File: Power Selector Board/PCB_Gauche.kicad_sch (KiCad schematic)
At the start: 23 parts, among them J101 MSD-DB01M-12P, J102 MSD-DB01F-12P_1, J103 64900221122, J104 64900221122, J105 64900221122, J106 1998865, K101 G6SK-2G DC24, K102 J115F11C24VDCSH.9, K103 J115F11C24VDCSH.9, U102 LMW78_24-0.3RL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

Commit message: Premier commit pour routing PCB. Modif footprint connecteur batterie.
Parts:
- added H1 (x4): Mounting-Hole-M3, Connectors:Mounting_Hole_3mm, symbol Mechanicals:Mounting-Hole-M3
- F101, F102: Current Rating (A) 30A -> 6.3A
- J101, J102: footprint Connectors:649012227222 -> Connectors:MSD-DB01F-12P-V2.0
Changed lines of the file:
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@@
       (effects (font (size 1.524 1.524)))
     )
-    (property "Footprint" "Connectors:649012227222" (at 335.28 146.05 0)
+    (property "Footprint" "Connectors:MSD-DB01F-12P-V2.0" (at 335.28 146.05 0)
       (effects (font (size 1.524 1.524)) hide)
     )
@@
     )
   )
+  (symbol (lib_id "Mechanicals:Mounting-Hole-M3") (at 58.42 203.2 0) (unit 1)
+    (in_bom yes) (on_board yes) (dnp no) (fields_autoplaced)
+    (property "Reference" "H1" (at 63.5 201.93 0)
+      (effects (font (size 1.524 1.524)) (justify left))
+    )
+    (property "Value" "Mounting-Hole-M3" (at 63.5 204.47 0)
+      (effects (font (size 1.524 1.524)) (justify left))
+    )
+    (property "Footprint" "Connectors:Mounting_Hole_3mm" (at 58.42 217.17 0)
+      (effects (font (size 1.524 1.524)) hide)
+    )
+    (property "Datasheet" "" (at 58.42 208.28 0)
+      (effects (font (size 1.524 1.524)) hide)
+    )
+    (pin "1")
+    (instances
+      (project "Power Selector"
+        (path "/809bdac1-fe7e-479d-b3c2-abd6ebce72b5/01a8522b-18e6-465b-b2cb-1d0f4aea8e80"
+          (reference "H1") (unit 1)
+        )
+        (path "/809bdac1-fe7e-479d-b3c2-abd6ebce72b5/c8dd6968-27fd-46e9-bc25-cf95ac0a1b0e"
+          (reference "H6") (unit 1)
+        )
+      )
+    )
+  )
   (symbol (lib_id "Power_Port:GND_G") (at 187.96 226.06 0) (unit 1)
     (in_bom yes) (on_board yes) (dnp no)
@@
         (path "/809bdac1-fe7e-479d-b3c2-abd6ebce72b5/c8dd6968-27fd-46e9-bc25-cf95ac0a1b0e"
           (reference "#PWR0205") (unit 1)
+        )
+      )
+    )
+  )
+  (symbol (lib_id "Mechanicals:Mounting-Hole-M3") (at 58.42 215.9 0) (unit 1)
+    (in_bom yes) (on_board yes) (dnp no) (fields_autoplaced)
+    (property "Reference" "H1" (at 63.5 214.63 0)
+      (effects (font (size 1.524 1.524)) (justify left))
+    )
+    (property "Value" "Mounting-Hole-M3" (at 63.5 217.17 0)
+      (effects (font (size 1.524 1.524)) (justify left))
+    )
+    (property "Footprint" "Connectors:Mounting_Hole_3mm" (at 58.42 229.87 0)
+      (effects (font (size 1.524 1.524)) hide)
+    )
+    (property "Datasheet" "" (at 58.42 220.98 0)
+      (effects (font (size 1.524 1.524)) hide)
+    )
+    (pin "1")
+    (instances
+      (project "Power Selector"
+        (path "/809bdac1-fe7e-479d-b3c2-abd6ebce72b5/01a8522b-18e6-465b-b2cb-1d0f4aea8e80"
+          (reference "H1") (unit 1)
+        )
+        (path "/809bdac1-fe7e-479d-b3c2-abd6ebce72b5/c8dd6968-27fd-46e9-bc25-cf95ac0a1b0e"
+          (reference "H7") (unit 1)
         )
       )
@@
       (effects (font (size 1.524 1.524)))
     )
-    (property "Footprint" "Connectors:649012227222" (at 53.34 153.67 0)
+    (property "Footprint" "Connectors:MSD-DB01F-12P-V2.0" (at 53.34 153.67 0)
       (effects (font (size 1.524 1.524)) hide)
     )
@@
       (effects (font (size 1.524 1.524)) hide)
     )
-    (property "Current Rating (A)" "30A" (at 67.31 72.39 0)
+    (property "Current Rating (A)" "6.3A" (at 67.31 72.39 0)
       (effects (font (size 1.27 1.27)))
     )
@@
     )
   )
+  (symbol (lib_id "Mechanicals:Mounting-Hole-M3") (at 58.42 228.6 0) (unit 1)
+    (in_bom yes) (on_board yes) (dnp no) (fields_autoplaced)
+    (property "Reference" "H1" (at 63.5 227.33 0)
+      (effects (font (size 1.524 1.524)) (justify left))
+    )
+    (property "Value" "Mounting-Hole-M3" (at 63.5 229.87 0)
+      (effects (font (size 1.524 1.524)) (justify left))
+    )
+    (property "Footprint" "Connectors:Mounting_Hole_3mm" (at 58.42 242.57 0)
+      (effects (font (size 1.524 1.524)) hide)
+    )
+    (property "Datasheet" "" (at 58.42 233.68 0)
+      (effects (font (size 1.524 1.524)) hide)
+    )
+    (pin "1")
+    (instances
+      (project "Power Selector"
+        (path "/809bdac1-fe7e-479d-b3c2-abd6ebce72b5/01a8522b-18e6-465b-b2cb-1d0f4aea8e80"
+          (reference "H1") (unit 1)
+        )
+        (path "/809bdac1-fe7e-479d-b3c2-abd6ebce72b5/c8dd6968-27fd-46e9-bc25-cf95ac0a1b0e"
+          (reference "H8") (unit 1)
+        )
+      )
+    )
+  )
   (symbol (lib_id "Power_Port:+24V_Tether_G") (at 133.35 95.25 0) (unit 1)
     (in_bom yes) (on_board yes) (dnp no)
@@
     )
   )
+  (symbol (lib_id "Mechanicals:Mounting-Hole-M3") (at 58.42 190.5 0) (unit 1)
+    (in_bom yes) (on_board yes) (dnp no) (fields_autoplaced)
+    (property "Reference" "H1" (at 63.5 189.23 0)
+      (effects (font (size 1.524 1.524)) (justify left))
+    )
+    (property "Value" "Mounting-Hole-M3" (at 63.5 191.77 0)
+      (effects (font (size 1.524 1.524)) (justify left))
+    )
+    (property "Footprint" "Connectors:Mounting_Hole_3mm" (at 58.42 204.47 0)
+      (effects (font (size 1.524 1.524)) hide)
+    )
+    (property "Datasheet" "" (at 58.42 195.58 0)
+      (effects (font (size 1.524 1.524)) hide)
+    )
+    (pin "1")
+    (instances
+      (project "Power Selector"
+        (path "/809bdac1-fe7e-479d-b3c2-abd6ebce72b5/01a8522b-18e6-465b-b2cb-1d0f4aea8e80"
+          (reference "H1") (unit 1)
+        )
+        (path "/809bdac1-fe7e-479d-b3c2-abd6ebce72b5/c8dd6968-27fd-46e9-bc25-cf95ac0a1b0e"
+          (reference "H5") (unit 1)
+        )
+      )
+    )
+  )
   (symbol (lib_id "Power_Port:+Vin_Bat_G") (at 78.74 102.87 0) (unit 1)
     (in_bom yes) (on_board yes) (dnp no)
@@
       (effects (font (size 1.524 1.524)) hide)
     )
-    (property "Current Rating (A)" "30A" (at 69.85 101.6 0)
-      (effects (font (size 1.27 1.27)))
-    )
+    (property "Current Rating (A)" "6.3A" (at 69.85 101.6 0)
+      (effects (font (size 1.27 1.27)))
+    )

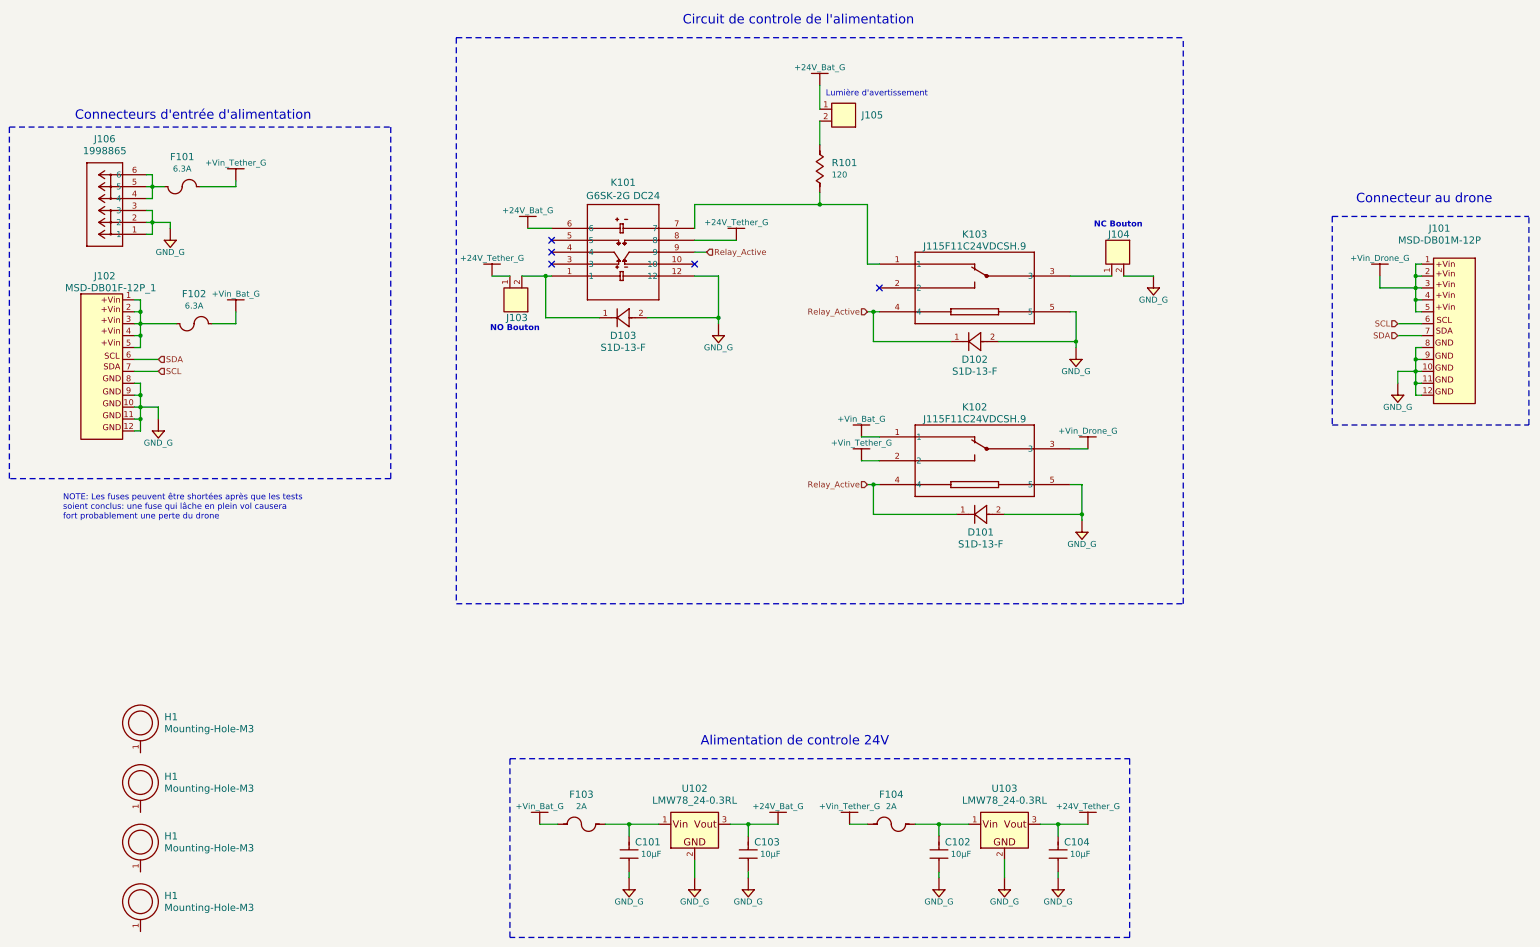
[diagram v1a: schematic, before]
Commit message: Ajout testpoints au schéma et PCB. Ajout de commentaires sur le silkscreen.
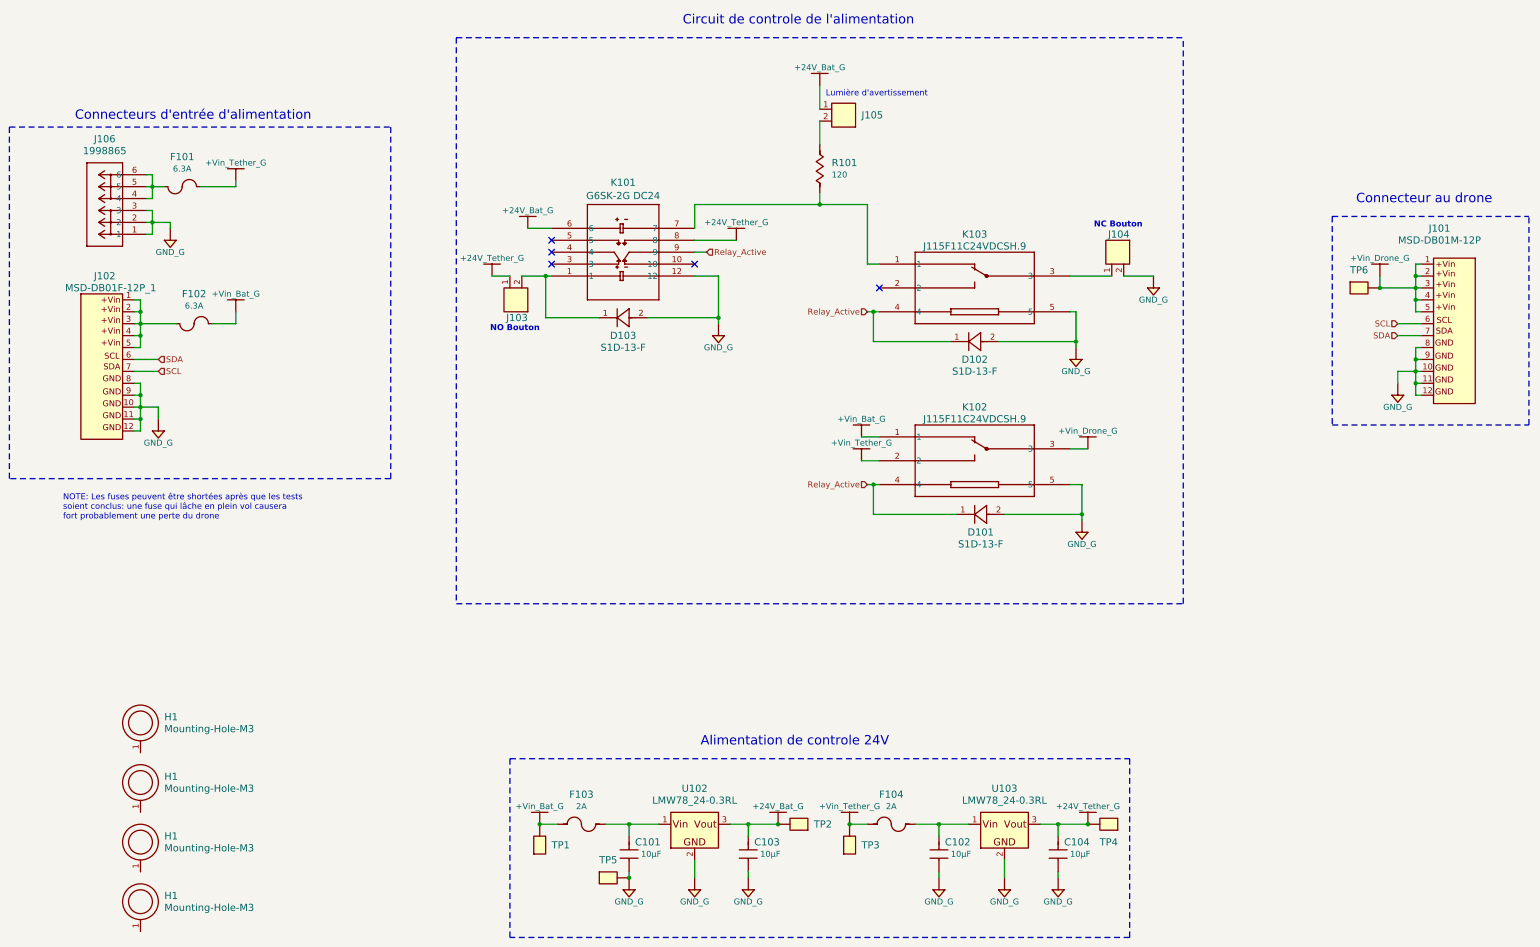
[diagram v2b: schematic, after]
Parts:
- added TP1: Vin Bat, Connectors:Keystone_5001, symbol Connectors:Test_Point_THM
- added TP2: 24V Bat, Connectors:Keystone_5001, symbol Connectors:Test_Point_THM
- added TP3: Vin Tether, Connectors:Keystone_5001, symbol Connectors:Test_Point_THM
- added TP4: 24V Tether, Connectors:Keystone_5001, symbol Connectors:Test_Point_THM
- added TP5: GND, Connectors:Keystone_5001, symbol Connectors:Test_Point_THM
- added TP6: Vout Drone, Connectors:Keystone_5001, symbol Connectors:Test_Point_THM
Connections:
- net +Vin_Drone_G: now also TP6.1 (TP)
- net +Vin_Tether_G: now also TP3.1 (TP)
- net 24V_Bat_G: now also TP2.1 (TP)
- net 24V_Tether_G: now also TP4.1 (TP)
- net GND_G: now also TP5.1 (TP)
- net Vin_Bat_G: now also TP1.1 (TP)
